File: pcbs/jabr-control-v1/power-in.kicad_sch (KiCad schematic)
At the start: 13 parts, among them J9001 43045-0201, U301 TVS3301DRBR, U302 TPS26600RHFR

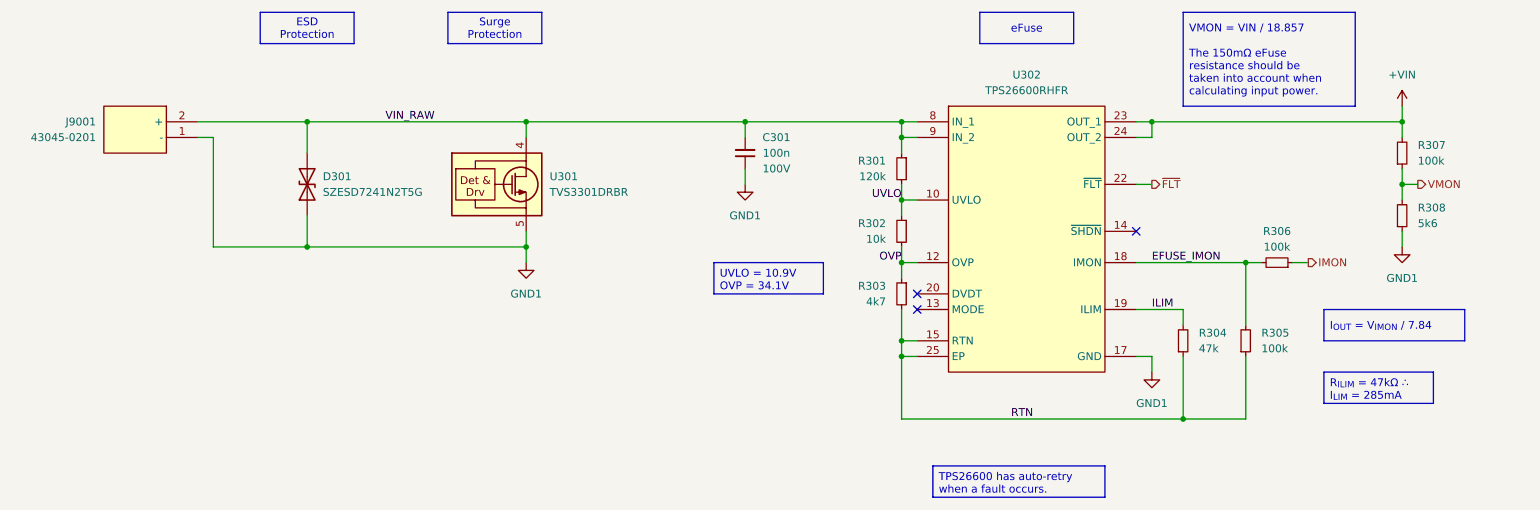
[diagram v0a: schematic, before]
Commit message: Added power sheets
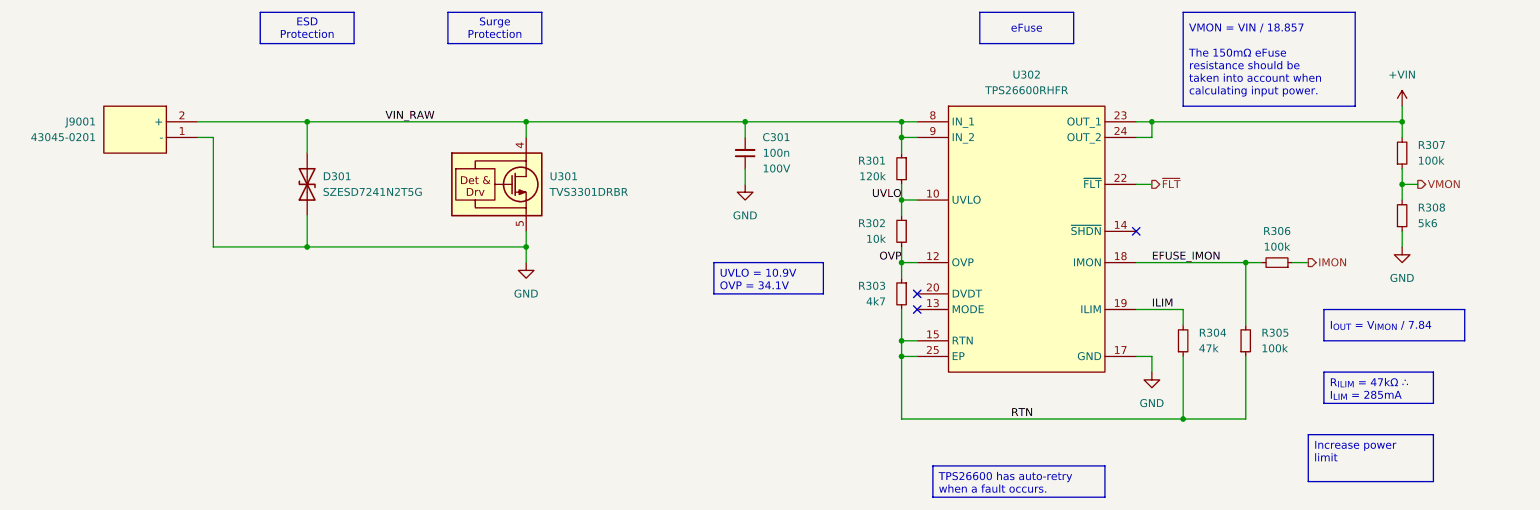
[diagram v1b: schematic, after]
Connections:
- net GND1 renamed GND
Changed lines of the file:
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@@
+		)
+	)
+	(text_box "Increase power limit"
+		(exclude_from_sim no)
+		(at 241.3 127 0)
+		(size 20.32 7.62)
+		(margins 0.9525 0.9525 0.9525 0.9525)
+		(stroke
+			(width 0)
+			(type solid)
+			(color 255 0 0 1)
+		)
+		(fill
+			(type none)
+		)
+		(effects
+			(font
+				(size 1.27 1.27)
+				(color 255 0 0 1)
+			)
+			(justify left top)
 		)
 	)
@@
 	)
 	(symbol
-		(lib_id "power:GND1")
+		(lib_id "power:GND")
 		(at 114.3 99.06 0)
 		(unit 1)
@@
 		(dnp no)
 		(fields_autoplaced yes)
-		(property "Reference" "#PWR0301"
+		(property "Reference" "#PWR301"
 			(at 114.3 105.41 0)
 			(effects
@@
 			)
 		)
-		(property "Value" "GND1"
+		(property "Value" "GND"
 			(at 114.3 104.14 0)
 			(effects
@@
 			)
 		)
-		(property "Description" "Power symbol creates a global label with name \"GND1\" , ground"
+		(property "Description" "Power symbol creates a global label with name \"GND\" , ground"
 			(at 114.3 99.06 0)
 			(effects
@@
 			(project "jabr-control-v1"
 				(path "/f91ec272-d09a-4038-bbbb-962739a92c51/3f551047-3bb0-4f63-99e0-34fd9061d844/c8847476-18c7-4518-a86a-3cbd7effb778"
-					(reference "#PWR0301")
+					(reference "#PWR301")
 					(unit 1)
 				)
@@
 	)
 	(symbol
-		(lib_id "power:GND1")
+		(lib_id "power:GND")
 		(at 149.86 86.36 0)
 		(unit 1)
@@
 		(dnp no)
 		(fields_autoplaced yes)
-		(property "Reference" "#PWR0302"
+		(property "Reference" "#PWR302"
 			(at 149.86 92.71 0)
 			(effects
@@
 			)
 		)
-		(property "Value" "GND1"
+		(property "Value" "GND"
 			(at 149.86 91.44 0)
 			(effects
@@
 			)
 		)
-		(property "Description" "Power symbol creates a global label with name \"GND1\" , ground"
+		(property "Description" "Power symbol creates a global label with name \"GND\" , ground"
 			(at 149.86 86.36 0)
 			(effects
@@
 			(project "jabr-control-v1"
 				(path "/f91ec272-d09a-4038-bbbb-962739a92c51/3f551047-3bb0-4f63-99e0-34fd9061d844/c8847476-18c7-4518-a86a-3cbd7effb778"
-					(reference "#PWR0302")
+					(reference "#PWR302")
 					(unit 1)
 				)
@@
 	)
 	(symbol
-		(lib_id "power:GND1")
+		(lib_id "power:GND")
 		(at 256.54 96.52 0)
 		(unit 1)
@@
 		(dnp no)
 		(fields_autoplaced yes)
-		(property "Reference" "#PWR0305"
+		(property "Reference" "#PWR305"
 			(at 256.54 102.87 0)
 			(effects
@@
 			)
 		)
-		(property "Value" "GND1"
+		(property "Value" "GND"
 			(at 256.54 101.6 0)
 			(effects
@@
 			)
 		)
-		(property "Description" "Power symbol creates a global label with name \"GND1\" , ground"
+		(property "Description" "Power symbol creates a global label with name \"GND\" , ground"
 			(at 256.54 96.52 0)
 			(effects
@@
 			(project "jabr-control-v1"
 				(path "/f91ec272-d09a-4038-bbbb-962739a92c51/3f551047-3bb0-4f63-99e0-34fd9061d844/c8847476-18c7-4518-a86a-3cbd7effb778"
-					(reference "#PWR0305")
+					(reference "#PWR305")
 					(unit 1)
 				)
@@
 	)
 	(symbol
-		(lib_id "power:GND1")
+		(lib_id "power:GND")
 		(at 215.9 116.84 0)
 		(unit 1)
@@
 		(dnp no)
 		(fields_autoplaced yes)
-		(property "Reference" "#PWR0303"
+		(property "Reference" "#PWR303"
 			(at 215.9 123.19 0)
 			(effects
@@
 			)
 		)
-		(property "Value" "GND1"
+		(property "Value" "GND"
 			(at 215.9 121.92 0)
 			(effects
@@
 			)
 		)
-		(property "Description" "Power symbol creates a global label with name \"GND1\" , ground"
+		(property "Description" "Power symbol creates a global label with name \"GND\" , ground"
 			(at 215.9 116.84 0)
 			(effects
@@
 			(project "jabr-control-v1"
 				(path "/f91ec272-d09a-4038-bbbb-962739a92c51/3f551047-3bb0-4f63-99e0-34fd9061d844/c8847476-18c7-4518-a86a-3cbd7effb778"
-					(reference "#PWR0303")
+					(reference "#PWR303")
 					(unit 1)
 				)

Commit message: Worked on power and other areas of the schematic
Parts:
- removed R305, R306, R307: 100k, Resistor_SMD:R_0402_1005Metric, symbol Device:R_Small
- removed R308: 5k6, Resistor_SMD:R_0402_1005Metric, symbol Device:R_Small
- R301, R302, R303: footprint Resistor_SMD:R_0402_1005Metric -> project_footprints:R_0402
- R304: value 47k -> 10k; footprint Resistor_SMD:R_0402_1005Metric -> project_footprints:R_0402
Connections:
- net EFUSE_IMON: no longer names the net of U302.18 (IMON)
- no-connect marks 3 -> 4
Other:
- moved on the sheet: C301, D301, J9001, R301, R302, R303, R304, U301, U302

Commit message: Schematic nearing completion, need to do GPIO and PHY decouplings caps
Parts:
- C301: footprint Capacitor_SMD:C_0603_1608Metric -> project_footprints:C_0603; symbol Device:C_Small -> DEV:C_SMALL
